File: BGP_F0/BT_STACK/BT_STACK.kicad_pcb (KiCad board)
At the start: 2 copper layers, 24 x 25 mm, 18 parts, among them P1 CONN_01X05, P2 CONN_01X02, P3 CONN_01X04, U1 MC33178

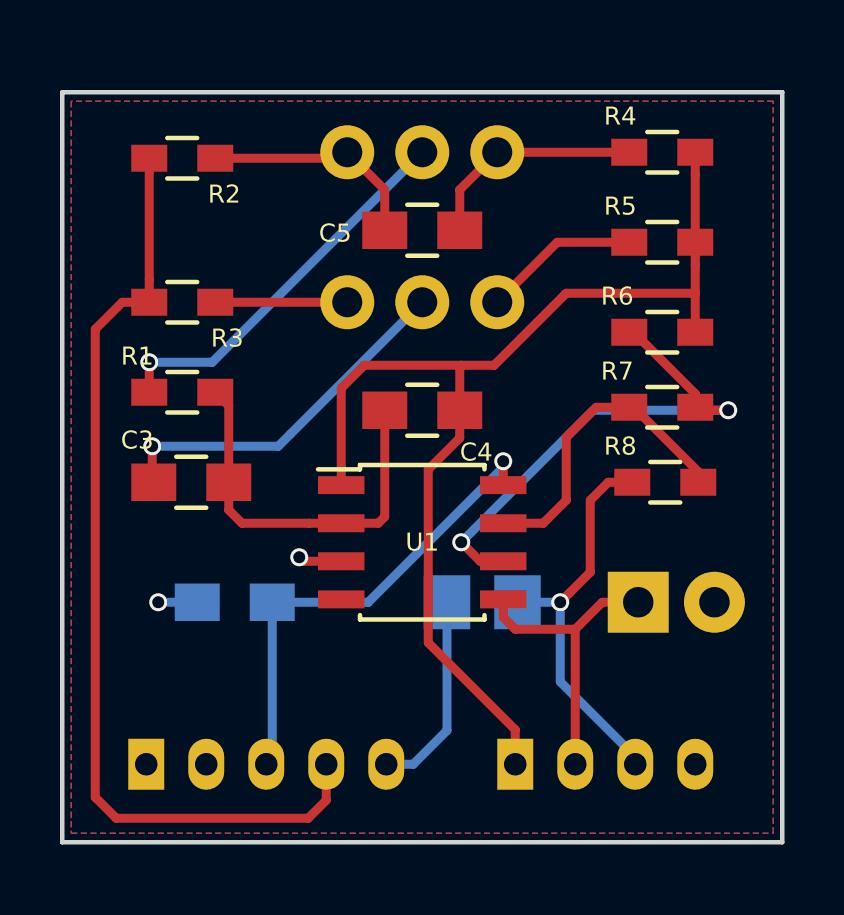
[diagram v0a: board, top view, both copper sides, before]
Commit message: F0 prot diode added, bt changed to 26mm
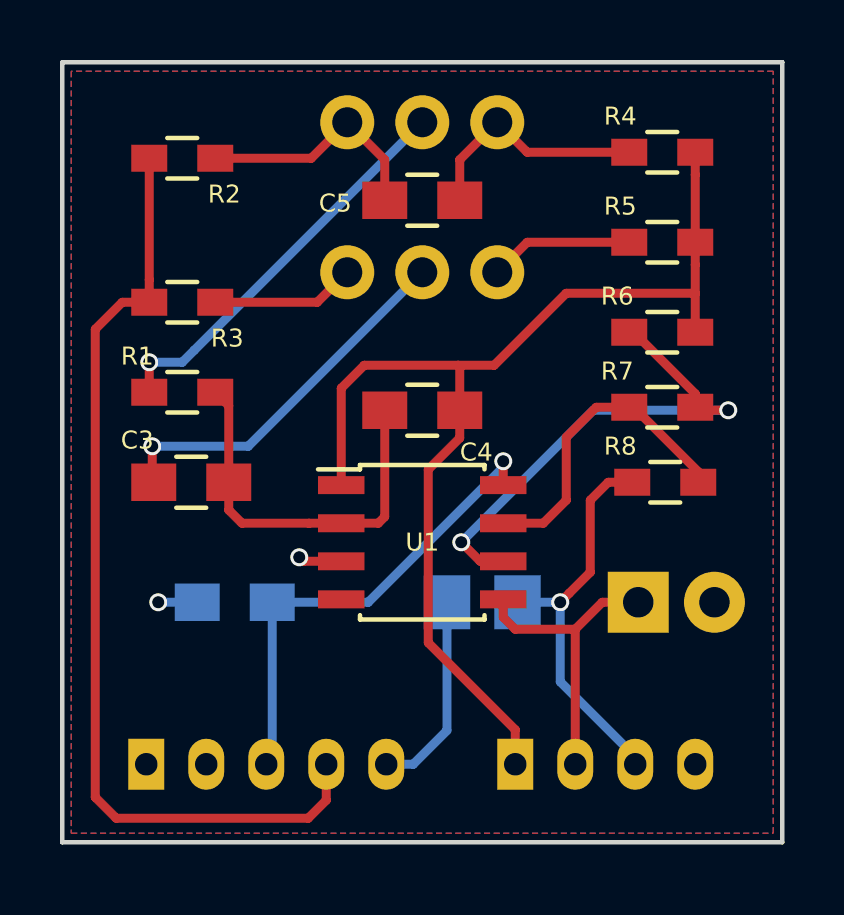
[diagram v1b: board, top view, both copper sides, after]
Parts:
- moved C5 1.00 mm to (152.0, 73.6)
- moved RV1 1.00 mm to (149.5, 71.0)
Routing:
- net /B-: track 7.60 -> 8.30 mm
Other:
- board size 24 x 25 mm -> 24 x 26 mm
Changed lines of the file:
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@@
-(kicad_pcb (version 4) (host pcbnew 4.0.4-1.fc24-product)
+(kicad_pcb (version 4) (host pcbnew 4.0.7)
   (general
     (links 34)
@@
     (thickness 1.6)
     (drawings 8)
-    (tracks 113)
+    (tracks 115)
     (zones 0)
     (modules 18)
@@
   )
   (module Capacitors_SMD:C_0805_HandSoldering (layer F.Cu)
-    (at 152 74.6 180)
+    (at 152 73.6 180)
     (descr "Capacitor SMD 0805, hand soldering")
     (tags "capacitor 0805")
@@
   )
   (module LIBS:Potentiometer_Alps_RK097_Double_Vertical_Dual_Shaft (layer B.Cu)
-    (at 149.5 72 90)
+    (at 149.5 71 90)
     (descr "Potentiometer, vertically mounted, Omeg PC16PU, Omeg PC16PU, Omeg PC16PU, Vishay/Spectrol 248GJ/249GJ Single, Vishay/Spectrol 248GJ/249GJ Single, Vishay/Spectrol 248GJ/249GJ Single, Vishay/Spectrol 248GH/249GH Single, Vishay/Spectrol 148/149 Single, Vishay/Spectrol 148/149 Single, Vishay/Spectrol 148/149 Single, Vishay/Spectrol 148A/149A Single with mounting plates, Vishay/Spectrol 148/149 Double, Vishay/Spectrol 148A/149A Double with mounting plates, Piher PC-16 Single, Piher PC-16 Single, Piher PC-16 Single, Piher PC-16SV Single, Piher PC-16 Double, Piher PC-16 Triple, Piher T16H Single, Piher T16L Single, Piher T16H Double, Alps RK163 Single, Alps RK163 Double, Alps RK097 Single, Alps RK097 Double, http://www.alps.com/prod/info/E/HTML/Potentiometer/RotaryPotentiometers/RK097/RK09712100AV.html")
     (tags "Potentiometer vertical  Omeg PC16PU  Omeg PC16PU  Omeg PC16PU  Vishay/Spectrol 248GJ/249GJ Single  Vishay/Spectrol 248GJ/249GJ Single  Vishay/Spectrol 248GJ/249GJ Single  Vishay/Spectrol 248GH/249GH Single  Vishay/Spectrol 148/149 Single  Vishay/Spectrol 148/149 Single  Vishay/Spectrol 148/149 Single  Vishay/Spectrol 148A/149A Single with mounting plates  Vishay/Spectrol 148/149 Double  Vishay/Spectrol 148A/149A Double with mounting plates  Piher PC-16 Single  Piher PC-16 Single  Piher PC-16 Single  Piher PC-16SV Single  Piher PC-16 Double  Piher PC-16 Triple  Piher T16H Single  Piher T16L Single  Piher T16H Double  Alps RK163 Single  Alps RK163 Double  Alps RK097 Single  Alps RK097 Double Dual Shaft")
@@
     )
   )
-  (gr_line (start 163.7 94.7) (end 163.7 70.3) (layer Margin) (width 0.2))
+  (gr_line (start 163.7 94.7) (end 163.7 69.3) (layer Margin) (width 0.2))
   (gr_line (start 140.3 94.7) (end 163.7 94.7) (layer Margin) (width 0.2))
-  (gr_line (start 140.3 70.3) (end 140.3 94.7) (layer Margin) (width 0.2))
-  (gr_line (start 163.7 70.3) (end 140.3 70.3) (layer Margin) (width 0.2))
-  (gr_line (start 164 95) (end 164 70) (layer Edge.Cuts) (width 0.15))
+  (gr_line (start 140.3 69.3) (end 140.3 94.7) (layer Margin) (width 0.2))
+  (gr_line (start 163.7 69.3) (end 140.3 69.3) (layer Margin) (width 0.2))
+  (gr_line (start 164 95) (end 164 69) (layer Edge.Cuts) (width 0.15))
   (gr_line (start 140 95) (end 164 95) (layer Edge.Cuts) (width 0.15))
-  (gr_line (start 140 70) (end 140 95) (layer Edge.Cuts) (width 0.15))
-  (gr_line (start 164 70) (end 140 70) (layer Edge.Cuts) (width 0.15))
+  (gr_line (start 140 69) (end 140 95) (layer Edge.Cuts) (width 0.15))
+  (gr_line (start 164 69) (end 140 69) (layer Edge.Cuts) (width 0.15))
   (segment (start 154.7 82.3) (end 154.7 82.5) (width 0.3) (layer B.Cu) (net 1))
   (segment (start 154.7 82.5) (end 150.2 87) (width 0.3) (layer B.Cu) (net 1))
@@
   (segment (start 152.82398 91.27602) (end 151.7 92.4) (width 0.3) (layer B.Cu) (net 4))
   (segment (start 151.7 92.4) (end 150.8 92.4) (width 0.3) (layer B.Cu) (net 4))
+  (segment (start 152 76) (end 146.2 81.8) (width 0.3) (layer B.Cu) (net 5))
+  (segment (start 146.2 81.8) (end 143 81.8) (width 0.3) (layer B.Cu) (net 5))
   (segment (start 143 81.8) (end 143 82.95) (width 0.3) (layer F.Cu) (net 5))
   (segment (start 143 82.95) (end 143.05 83) (width 0.3) (layer F.Cu) (net 5))
-  (segment (start 147.6 81.4) (end 147.2 81.8) (width 0.3) (layer B.Cu) (net 5))
-  (segment (start 147.2 81.8) (end 143 81.8) (width 0.3) (layer B.Cu) (net 5))
   (via (at 143 81.8) (size 0.6) (drill 0.4) (layers F.Cu B.Cu) (net 5))
-  (segment (start 152 77) (end 147.6 81.4) (width 0.3) (layer B.Cu) (net 5))
   (segment (start 150.75 84.15) (end 150.535 84.365) (width 0.3) (layer F.Cu) (net 6))
   (segment (start 150.535 84.365) (end 149.3 84.365) (width 0.3) (layer F.Cu) (net 6))
@@
   (segment (start 145.55 83) (end 145.55 80.45) (width 0.3) (layer F.Cu) (net 6))
   (segment (start 145.55 80.45) (end 145.1 80) (width 0.3) (layer F.Cu) (net 6))
+  (segment (start 153.2 79.1) (end 154.398002 79.1) (width 0.3) (layer F.Cu) (net 7))
+  (segment (start 154.398002 79.1) (end 156.798002 76.7) (width 0.3) (layer F.Cu) (net 7))
+  (segment (start 149.3 83.095) (end 149.3 79.864998) (width 0.3) (layer F.Cu) (net 7))
+  (segment (start 149.3 79.864998) (end 150.064998 79.1) (width 0.3) (layer F.Cu) (net 7))
+  (segment (start 150.064998 79.1) (end 153.2 79.1) (width 0.3) (layer F.Cu) (net 7))
+  (segment (start 153.2 79.1) (end 153.25 79.15) (width 0.3) (layer F.Cu) (net 7))
+  (segment (start 153.25 79.15) (end 153.25 80.6) (width 0.3) (layer F.Cu) (net 7))
   (segment (start 153.25 81.525) (end 152.2 82.575) (width 0.3) (layer F.Cu) (net 7))
   (segment (start 152.2 88.35) (end 155.1 91.25) (width 0.3) (layer F.Cu) (net 7))
@@
   (segment (start 155.1 91.25) (end 155.1 92.4) (width 0.3) (layer F.Cu) (net 7))
   (segment (start 152.2 82.575) (end 152.2 88.35) (width 0.3) (layer F.Cu) (net 7))
-  (segment (start 153.3 79.1) (end 150.064998 79.1) (width 0.3) (layer F.Cu) (net 7))
-  (segment (start 150.064998 79.1) (end 149.3 79.864998) (width 0.3) (layer F.Cu) (net 7))
-  (segment (start 149.3 79.864998) (end 149.3 82.495) (width 0.3) (layer F.Cu) (net 7))
-  (segment (start 149.3 82.495) (end 149.3 83.095) (width 0.3) (layer F.Cu) (net 7))
   (segment (start 161.1 76.7) (end 156.798002 76.7) (width 0.3) (layer F.Cu) (net 7))
-  (segment (start 156.798002 76.7) (end 154.398002 79.1) (width 0.3) (layer F.Cu) (net 7))
-  (segment (start 154.398002 79.1) (end 153.3 79.1) (width 0.3) (layer F.Cu) (net 7))
-  (segment (start 153.3 79.1) (end 153.25 79.15) (width 0.3) (layer F.Cu) (net 7))
-  (segment (start 153.25 79.15) (end 153.25 80.6) (width 0.3) (layer F.Cu) (net 7))
   (segment (start 161.1 76.7) (end 161.1 78) (width 0.3) (layer F.Cu) (net 7))
   (segment (start 161.1 75.75) (end 161.1 76.7) (width 0.3) (layer F.Cu) (net 7))
@@
   (segment (start 161.1 75) (end 161.1 75.75) (width 0.3) (layer F.Cu) (net 7))
   (segment (start 161.1 72) (end 161.25 72) (width 0.3) (layer F.Cu) (net 7))
-  (segment (start 153.25 74.6) (end 153.25 73.25) (width 0.3) (layer F.Cu) (net 8))
-  (segment (start 153.25 73.25) (end 154.5 72) (width 0.3) (layer F.Cu) (net 8))
+  (segment (start 158.9 72) (end 155.5 72) (width 0.3) (layer F.Cu) (net 8))
+  (segment (start 155.5 72) (end 154.5 71) (width 0.3) (layer F.Cu) (net 8))
+  (segment (start 153.25 73.6) (end 153.25 72.25) (width 0.3) (layer F.Cu) (net 8))
+  (segment (start 153.25 72.25) (end 154.5 71) (width 0.3) (layer F.Cu) (net 8))
   (segment (start 158.9 72) (end 159.05 72) (width 0.3) (layer F.Cu) (net 8))
-  (segment (start 158.9 72) (end 154.5 72) (width 0.3) (layer F.Cu) (net 8))
-  (segment (start 150.75 74.6) (end 150.75 73.25) (width 0.3) (layer F.Cu) (net 9))
-  (segment (start 150.75 73.25) (end 149.5 72) (width 0.3) (layer F.Cu) (net 9))
-  (segment (start 145.1 72.2) (end 149.3 72.2) (width 0.3) (layer F.Cu) (net 9))
-  (segment (start 149.3 72.2) (end 149.5 72) (width 0.3) (layer F.Cu) (net 9))
+  (segment (start 145.1 72.2) (end 148.3 72.2) (width 0.3) (layer F.Cu) (net 9))
+  (segment (start 148.3 72.2) (end 149.5 71) (width 0.3) (layer F.Cu) (net 9))
+  (segment (start 150.75 73.6) (end 150.75 72.25) (width 0.3) (layer F.Cu) (net 9))
+  (segment (start 150.75 72.25) (end 149.5 71) (width 0.3) (layer F.Cu) (net 9))
+  (segment (start 149.3 71.2) (end 149.5 71) (width 0.3) (layer F.Cu) (net 9))
   (segment (start 148.03501 85.635) (end 147.90001 85.5) (width 0.3) (layer F.Cu) (net 10))
   (segment (start 149.3 85.635) (end 148.03501 85.635) (width 0.3) (layer F.Cu) (net 10))
@@
   (segment (start 158 87) (end 157.1 87.9) (width 0.3) (layer F.Cu) (net 12))
   (segment (start 157.1 87.9) (end 157.1 92.4) (width 0.3) (layer F.Cu) (net 12))
+  (segment (start 142.9 79) (end 144 79) (width 0.3) (layer B.Cu) (net 13))
+  (segment (start 144 79) (end 144.4 78.6) (width 0.3) (layer B.Cu) (net 13))
+  (segment (start 144.4 78.6) (end 152 71) (width 0.3) (layer B.Cu) (net 13))
   (segment (start 142.9 79) (end 142.9 80) (width 0.3) (layer F.Cu) (net 13))
-  (segment (start 152 72) (end 145 79) (width 0.3) (layer B.Cu) (net 13))
   (via (at 142.9 79) (size 0.6) (drill 0.4) (layers F.Cu B.Cu) (net 13))
-  (segment (start 145 79) (end 142.9 79) (width 0.3) (layer B.Cu) (net 13))
-  (segment (start 145.1 77) (end 149.5 77) (width 0.3) (layer F.Cu) (net 14))
-  (segment (start 158.9 75) (end 156.5 75) (width 0.3) (layer F.Cu) (net 15))
-  (segment (start 156.5 75) (end 154.5 77) (width 0.3) (layer F.Cu) (net 15))
+  (segment (start 145.1 77) (end 148.5 77) (width 0.3) (layer F.Cu) (net 14))
+  (segment (start 148.5 77) (end 149.5 76) (width 0.3) (layer F.Cu) (net 14))
+  (segment (start 158.9 75) (end 155.5 75) (width 0.3) (layer F.Cu) (net 15))
+  (segment (start 155.5 75) (end 154.5 76) (width 0.3) (layer F.Cu) (net 15))
   (segment (start 162.2 80.6) (end 161.2 80.6) (width 0.3) (layer F.Cu) (net 16))
   (segment (start 161.2 80.6) (end 161.1 80.5) (width 0.3) (layer F.Cu) (net 16))
@@
     (polygon
       (pts
-        (xy 163.7 70.3) (xy 140.3 70.3) (xy 140.3 94.7) (xy 163.7 94.7)
+        (xy 163.7 69.3) (xy 140.3 69.3) (xy 140.3 94.7) (xy 163.7 94.7)
       )
     )
@@
     (polygon
       (pts
-        (xy 163.7 70.3) (xy 140.3 70.3) (xy 140.3 94.7) (xy 163.7 94.7)
+        (xy 163.7 69.3) (xy 140.3 69.3) (xy 140.3 94.7) (xy 163.7 94.7)
       )
     )

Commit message: Removed old boards, all F0 are now 26mm deep
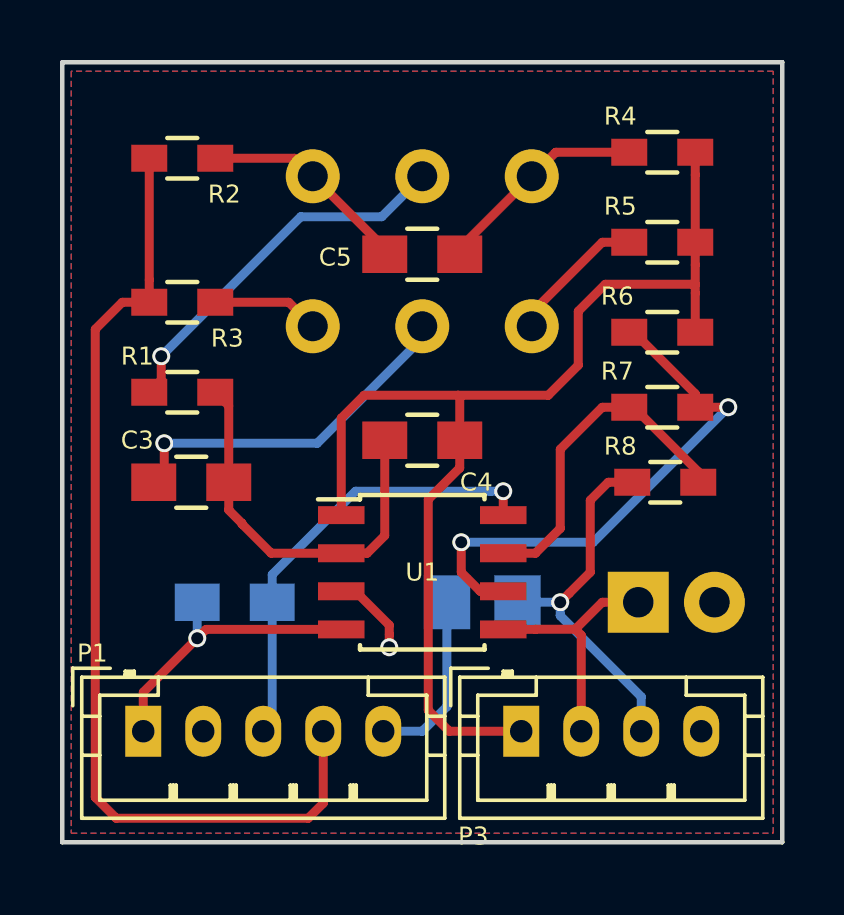
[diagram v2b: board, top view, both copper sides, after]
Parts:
- P1, P3: moved to F.Cu
- RV1: footprint LIBS:Potentiometer_Alps_RK097_Double_Vertical_Dual_Shaft -> LIBS:Potentiometer_Alpha_Double_Vertical_Dual_Shaft
- moved RV1 2.14 mm to (148.3, 72.8)
- moved C5 1.80 mm to (152.0, 75.4)
- moved P3 1.12 mm to (155.3, 91.3)
- moved P1 1.10 mm to (142.7, 91.3)
- moved C4 1.00 mm to (152.0, 81.6)
- moved U1 1.00 mm to (152.0, 86.0)
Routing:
- net Earth: track 1.43 -> 10.1 mm
- net /MID_R: track 10.1 -> 8.36 mm
- net /Vref: track 1.46 -> 2.81 mm
- net /T-: track 4.81 -> 3.58 mm
- net /B-: track 8.30 -> 7.09 mm
- net Net-(R6-Pad1): track 17.0 -> 18.2 mm
- net /MID_O: track 13.3 -> 12.3 mm
- net /MID_I: track 37.4 -> 38.4 mm
- net /BW: track 13.4 -> 12.6 mm
- net /V+: track 16.0 -> 15.2 mm
- net /OUT: track 6.77 -> 5.94 mm
- net /IN: track 32.4 -> 33.2 mm
- net /B+: track 8.08 -> 7.33 mm
- net Net-(R7-Pad1): track 10.6 -> 11.3 mm
- net /TW: track 12.6 -> 12.0 mm
- added copper zone on F.Cu, net (none)
- removed copper zone on F.Cu, net Earth

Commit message: BT and MID pot gain ctrl reversed for proper action
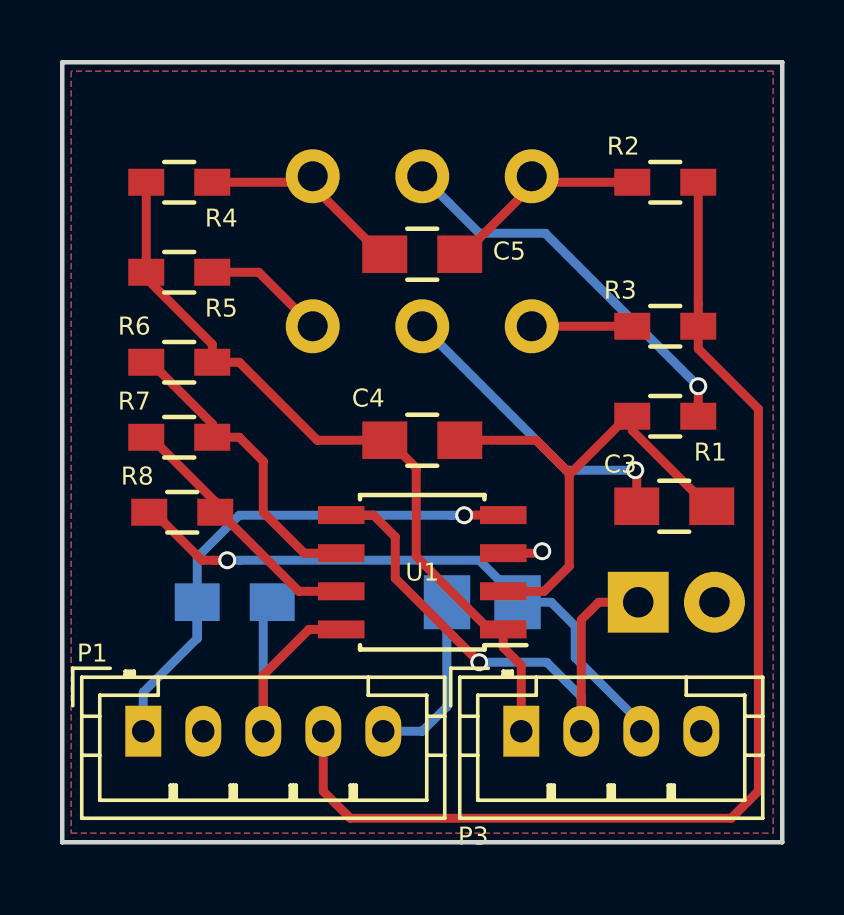
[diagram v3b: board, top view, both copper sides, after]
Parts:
- R2, R4: value 2.2k -> 4.7k
- moved R4 16.1 mm to (143.9, 73.0), turned to 0 degrees
- moved R5 16.1 mm to (143.9, 76.0), turned to 0 degrees
- moved R6 16.1 mm to (143.9, 79.0)
- moved R7 16.1 mm to (143.9, 81.5)
- moved R8 16.1 mm to (144.0, 84.0)
- moved C3 16.1 mm to (160.4, 83.8)
- moved R1 16.1 mm to (160.1, 80.8), turned to 180 degrees
- moved R2 16.1 mm to (160.1, 73.0), turned to 0 degrees
- moved R3 16.1 mm to (160.1, 77.8), turned to 0 degrees
- turned C4 to 0 degrees
- turned C5 to 0 degrees
- turned U1 to 180 degrees
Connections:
- C5 pad 1: /B+ -> /B-
- C5 pad 2: /B- -> /B+
- R2 pad 1: /B- -> /B+
- R3 pad 1: /T- -> /T+
- R4 pad 2: /B+ -> /B-
- R5 pad 2: /T+ -> /T-
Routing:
- net /MID_I: track 38.4 -> 25.7 mm
- net /MID_R: track 8.36 -> 18.3 mm, vias 0 -> 1
- net Earth: track 10.1 -> 18.5 mm
- net /MID_O: track 12.3 -> 20.3 mm
- net Net-(R6-Pad1): track 18.2 -> 10.4 mm, vias 2 -> 0
- net /V+: track 15.2 -> 9.53 mm, vias 1 -> 0
- net /IN: track 33.2 -> 38.4 mm
- net Net-(C3-Pad2): track 13.3 -> 16.8 mm
- net Net-(R7-Pad1): track 11.3 -> 8.83 mm
- net /TW: track 12.0 -> 10.3 mm
- net /Vref: track 2.81 -> 1.33 mm
- net /T+: track 4.67 -> 3.35 mm
- net /BW: track 12.6 -> 13.1 mm
- net /T-: track 3.58 -> 4.10 mm
